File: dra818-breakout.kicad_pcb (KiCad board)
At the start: 2 copper layers, 22.9 x 63.5 mm, 4 parts, among them J1 Conn_01x06, J2 Conn_01x05, U1 DRA818

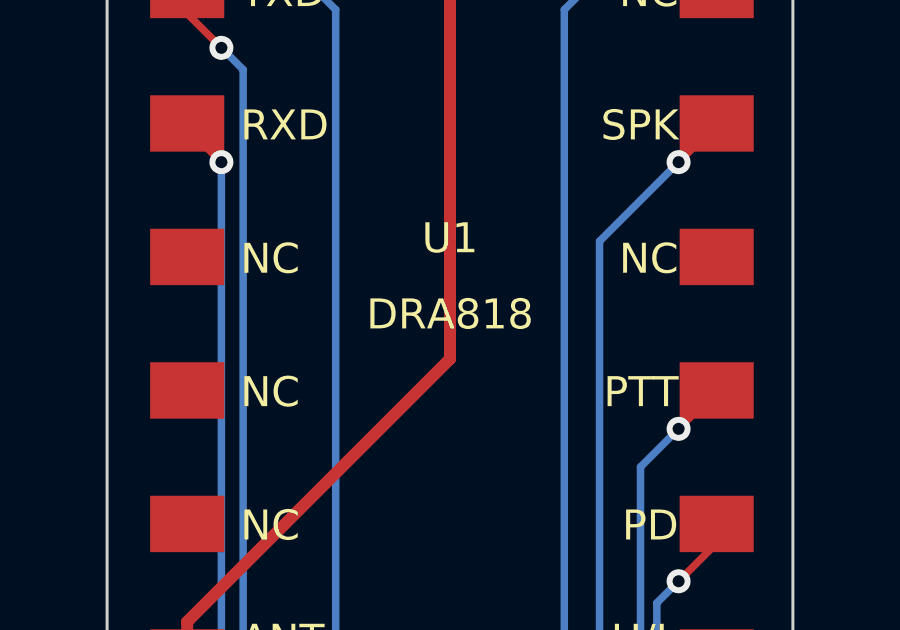
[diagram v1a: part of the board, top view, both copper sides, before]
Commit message: Add open hardware logo
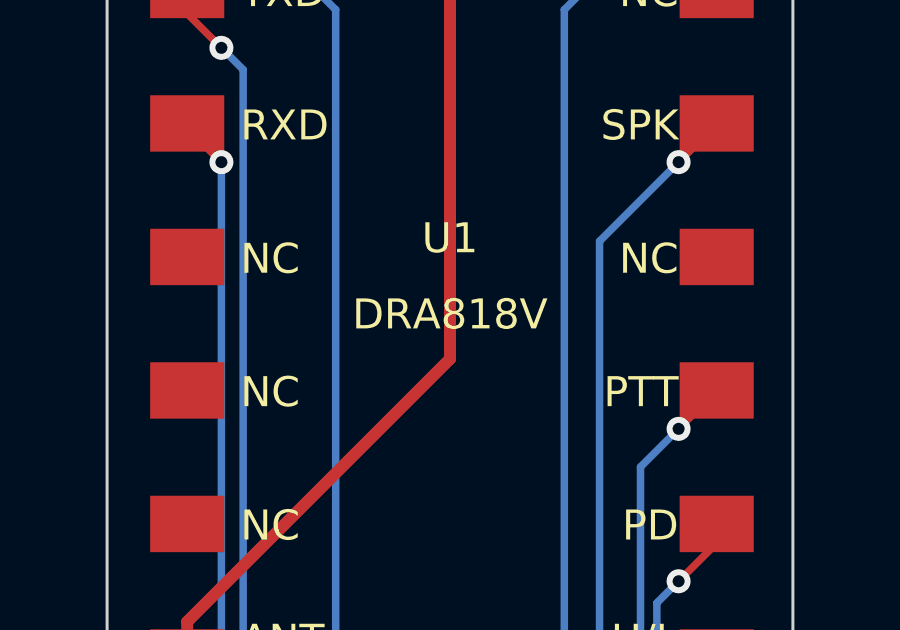
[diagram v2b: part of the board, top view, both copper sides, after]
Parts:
- added SYM1: Logo_Open_Hardware_Small, Symbol:OSHW-Logo2_7.3x6mm_SilkScreen, B.Cu at (151.0, 104.0)
- U1: value DRA818 -> DRA818V
